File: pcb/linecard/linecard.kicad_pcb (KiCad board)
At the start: 6 copper layers, 185 x 93.5 mm, 624 parts, among them J1 CONN_ATX12V, J10 ARF6-08-S-D-A-K-TR, J11 SMPM, J12 SMPM, J13 XILINX_JTAG, J14 ARF6-08-S-D-A-K-TR, J2 LPJT476156AENL, J3 CORTEX_DEBUG_ETM, J4 0532611071, J5 LPJT476156AENL, J6 XILINX_JTAG, J7 SMPM, J8 SMPM, J9 LPJT476156AENL, M1 LONGTHING, M10 SCREWHOLE, M11 SCREWHOLE, M12 960-27-12-D-AB-0, M13 960-27-12-D-AB-0, M2 OSHW, M3 WEEE, M4 SCREWHOLE, M5 SCREWHOLE, M6 SCREWHOLE, M7 SCREWHOLE, M8 SCREWHOLE, M9 SCREWHOLE, SW1 SWITCH, SW2 SWITCH, U1 MYMGK00504ERSR, U10 VSC8512, U11 ESD224DQAR, U12 ESD224DQAR, U13 ESD224DQAR, U14 ESD224DQAR, U15 ESD224DQAR, U16 ESD224DQAR, U17 ESD224DQAR, U18 ESD224DQAR, U19 ESD224DQAR, U2 MYMGK00504ERSR, U20 ESD224DQAR, U21 ESD224DQAR, U22 ESD224DQAR, U23 ESD224DQAR, U24 ESD224DQAR, U25 ESD224DQAR, U26 ESD224DQAR, U27 ESD224DQAR, U28 ESD224DQAR, U29 ESD224DQAR, U3 MYMGK00504ERSR, U30 ESD224DQAR, U31 ESD224DQAR, U32 ESD224DQAR, U33 ESD224DQAR, U34 ESD224DQAR, U35 VSC8512, U36 ESD224DQAR, U37 ESD224DQAR, U38 ESD224DQAR, U39 ESD224DQAR, U4 MYMGK00504ERSR, U40 ESD224DQAR, U41 ESD224DQAR, U42 ESD224DQAR, U43 ESD224DQAR, U44 ESD224DQAR, U45 ESD224DQAR, U46 ESD224DQAR, U47 ESD224DQAR, U48 ESD224DQAR, U49 ESD224DQAR, U5 STM32L431-QFN48, U50 ESD224DQAR, U51 ESD224DQAR, U52 ESD224DQAR, U53 ESD224DQAR, U54 ESD224DQAR, U55 ESD224DQAR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

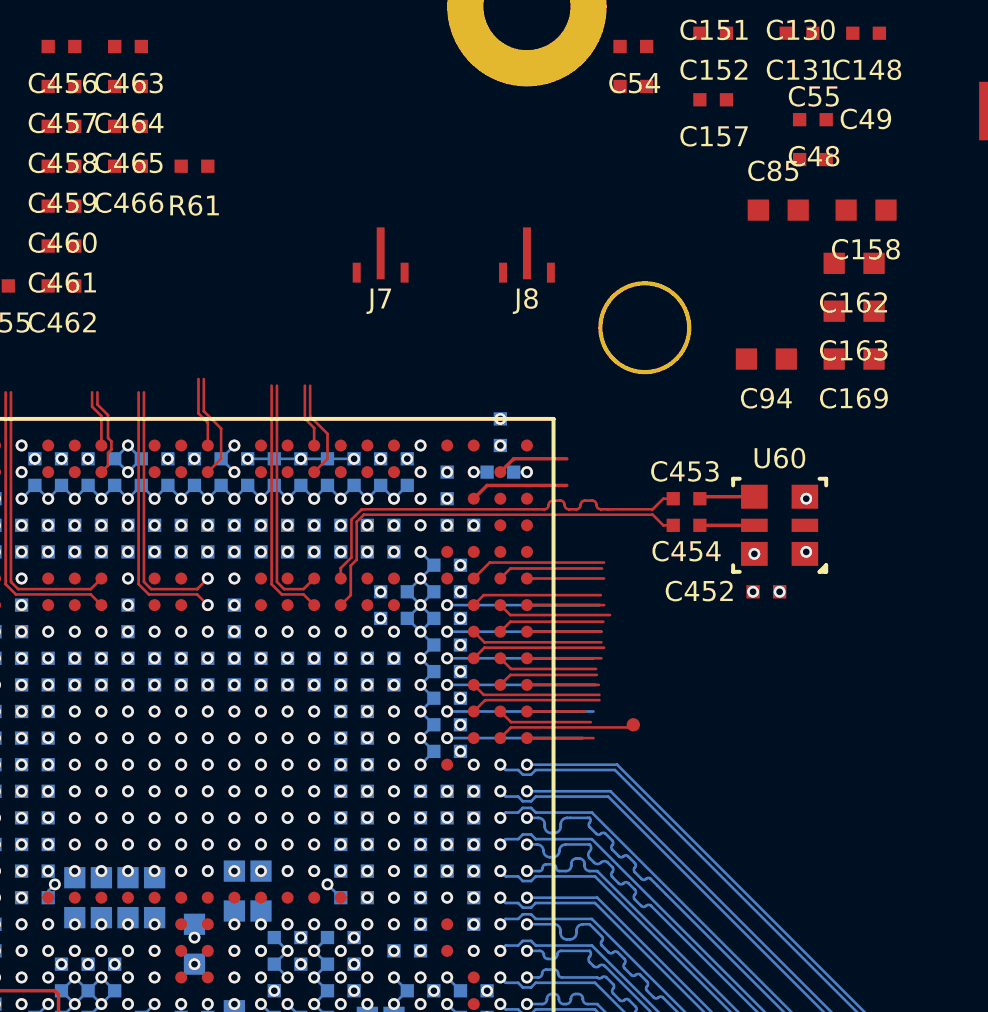
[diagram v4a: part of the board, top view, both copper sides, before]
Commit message: Finished routing LEDs to left PHY
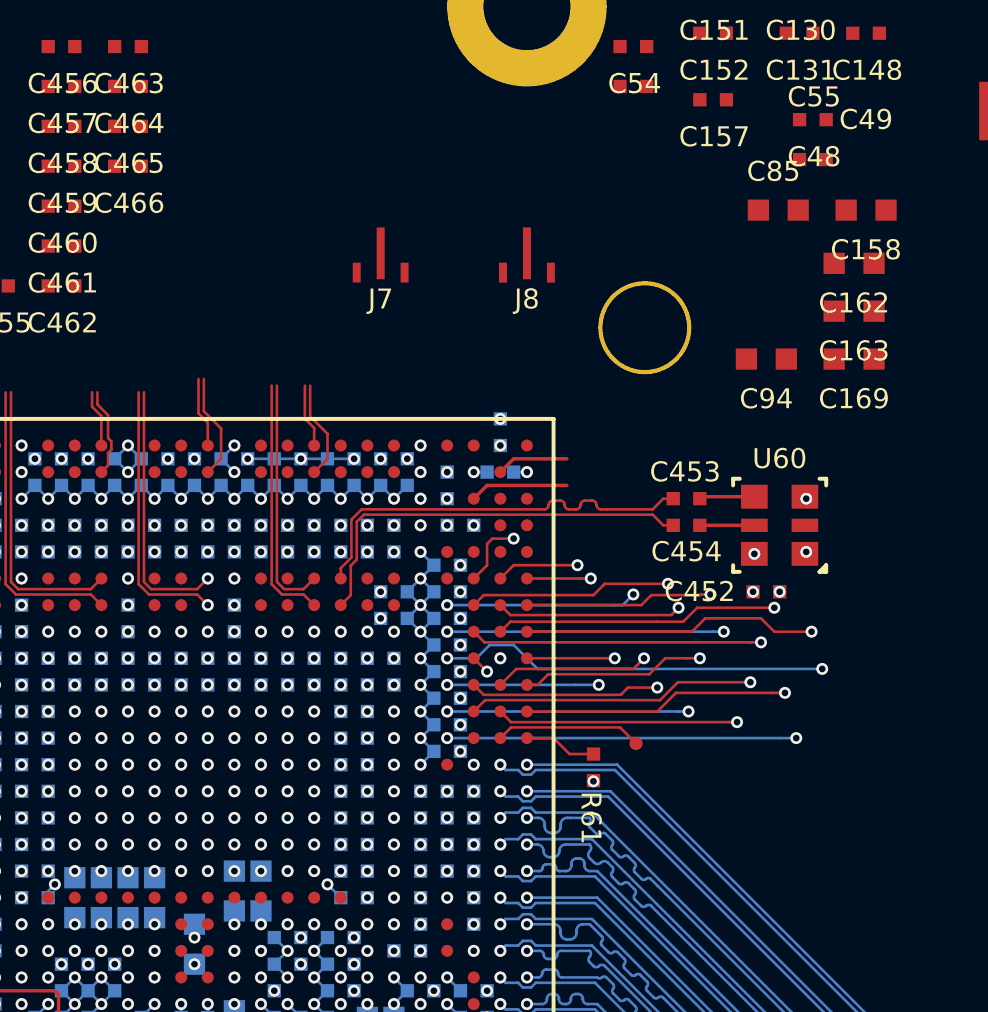
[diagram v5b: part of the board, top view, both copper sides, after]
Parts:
- moved R61 27.1 mm to (89.0, 88.1), turned to 90 degrees
- moved TP23 0.71 mm to (90.6, 87.2)
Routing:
- net Net-(U10B-PHY9_LED1): track 54.9 -> 72.2 mm, vias 1 -> 2
- net Net-(U10B-PHY10_LED1): track 55.8 -> 72.4 mm, vias 1 -> 2
- net Net-(U10B-PHY8_LED1): track 49.5 -> 65.4 mm, vias 1 -> 2
- net Net-(U10B-PHY10_LED0): track 54.9 -> 70.1 mm, vias 1 -> 2
- net Net-(U10B-PHY6_LED1): track 50.8 -> 65.6 mm, vias 1 -> 2
- net Net-(U10B-PHY8_LED0): track 55.3 -> 69.1 mm, vias 1 -> 2
- net Net-(U10B-PHY11_LED0): track 56.0 -> 69.7 mm, vias 2 -> 3
- net Net-(U10B-PHY7_LED1): track 60.4 -> 74.1 mm, vias 2 -> 3
- net Net-(U10B-PHY4_LED1): track 63.3 -> 76.5 mm, vias 1 -> 2
- net Net-(U10B-PHY5_LED1): track 67.2 -> 79.8 mm, vias 1 -> 2
- net Net-(U10B-PHY9_LED0): track 47.3 -> 59.5 mm, vias 1 -> 2
- net Net-(U10B-PHY6_LED0): track 56.3 -> 68.4 mm, vias 1 -> 2
- net Net-(U10B-PHY11_LED1): track 67.6 -> 79.5 mm, vias 2 -> 3
- net Net-(U10B-PHY3_LED1): track 83.1 -> 94.6 mm, vias 2 -> 3
- net Net-(U10B-PHY2_LED1): track 74.3 -> 84.8 mm, vias 1 -> 2
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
